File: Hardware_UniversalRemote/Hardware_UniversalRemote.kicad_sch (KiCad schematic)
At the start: 58 parts, among them J1 USB_B_Micro, Q1 S8050, Q2 BSS138, Q3 S8050, Q4 S8050, Q5 S8050, Q6 S8050, Q7 S8050, SW1 SW_Push, SW2 SW_Push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

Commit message: add first pcb layout version
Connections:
- net IO13: now also Q2.2 (S), R8.1, TP2.1; no longer C11.1, R16.2, SW3.1
- net IO16: now also C11.1, R16.2, SW3.1; no longer Q2.2 (S), R8.1, TP2.1
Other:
- moved on the sheet: TP2
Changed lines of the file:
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@@
 	(wire
 		(pts
+			(xy 86.36 137.16) (xy 100.33 137.16)
+		)
+		(stroke
+			(width 0)
+			(type default)
+		)
+	)
+	(wire
+		(pts
 			(xy 234.95 88.9) (xy 234.95 92.71)
 		)
@@
 	(wire
 		(pts
-			(xy 86.36 137.16) (xy 102.87 137.16)
-		)
-		(stroke
-			(width 0)
-			(type default)
-		)
-	)
-	(wire
-		(pts
 			(xy 250.19 140.97) (xy 250.19 142.24)
 		)
@@
 	)
 	(label "KEY"
-		(at 100.33 129.54 180)
+		(at 100.33 137.16 180)
 		(fields_autoplaced yes)
 		(effects
@@
 	)
 	(label "IRM"
-		(at 100.33 137.16 180)
+		(at 100.33 129.54 180)
 		(fields_autoplaced yes)
 		(effects
@@
 	(symbol
 		(lib_id "Connector:TestPoint")
-		(at 102.87 137.16 270)
+		(at 100.33 129.54 270)
 		(unit 1)
 		(exclude_from_sim no)
@@
 		(fields_autoplaced yes)
 		(property "Reference" "TP2"
-			(at 107.95 135.8899 90)
+			(at 105.41 128.2699 90)
 			(effects
 				(font
@@
 		)
 		(property "Value" "TestPoint"
-			(at 107.95 138.4299 90)
+			(at 105.41 130.8099 90)
 			(effects
 				(font
@@
 		)
 		(property "Footprint" "TestPoint:TestPoint_Pad_D2.5mm"
-			(at 102.87 142.24 0)
+			(at 100.33 134.62 0)
 			(effects
 				(font
@@
 		)
 		(property "Datasheet" "~"
-			(at 102.87 142.24 0)
+			(at 100.33 134.62 0)
 			(effects
 				(font
@@
 		)
 		(property "Description" "test point"
-			(at 102.87 137.16 0)
+			(at 100.33 129.54 0)
 			(effects
 				(font

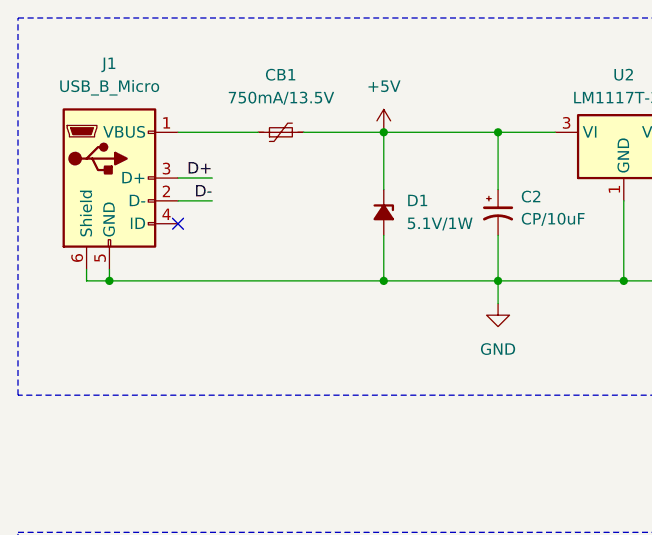
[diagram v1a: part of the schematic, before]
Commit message: modify layout
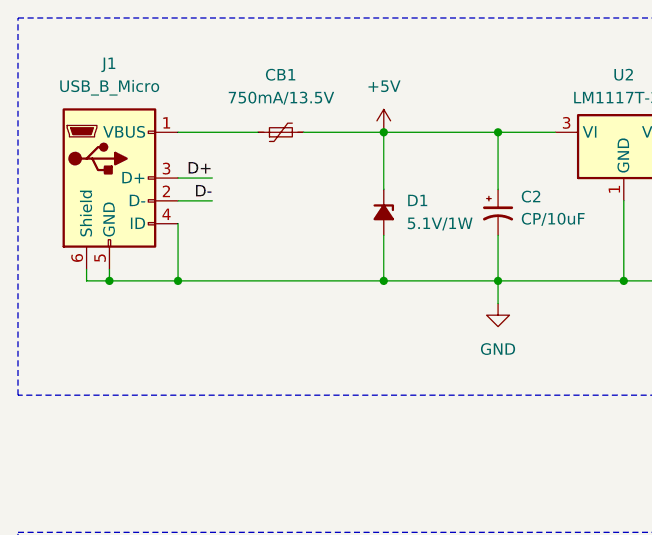
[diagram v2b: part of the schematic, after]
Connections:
- net GND: now also J1.4 (ID)
- no-connect marks 29 -> 28
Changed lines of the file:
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@@
+	)
+	(junction
+		(at 39.37 46.99)
+		(diameter 0)
+		(color 0 0 0 0)
 	)
 	(junction
@@
 	)
 	(no_connect
-		(at 39.37 40.64)
-	)
-	(no_connect
 		(at 95.25 162.56)
 	)
@@
 	(wire
 		(pts
+			(xy 39.37 40.64) (xy 39.37 46.99)
+		)
+		(stroke
+			(width 0)
+			(type default)
+		)
+	)
+	(wire
+		(pts
 			(xy 160.02 165.1) (xy 160.02 154.94)
 		)
@@
 	(wire
 		(pts
+			(xy 39.37 46.99) (xy 31.75 46.99)
+		)
+		(stroke
+			(width 0)
+			(type default)
+		)
+	)
+	(wire
+		(pts
 			(xy 142.24 95.25) (xy 142.24 97.79)
 		)
@@
 	(wire
 		(pts
-			(xy 62.23 46.99) (xy 31.75 46.99)
-		)
-		(stroke
+			(xy 62.23 46.99) (xy 39.37 46.99)
+		)
+		(stroke

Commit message: modify routing
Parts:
- D4, D5, D6, D7, D8, D9: footprint LED_THT:LED_D5.0mm -> LED_THT:LED_D5.0mm_Horizontal_O3.81mm_Z9.0mm
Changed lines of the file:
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@@
 			)
 		)
-		(property "Footprint" "LED_THT:LED_D5.0mm"
+		(property "Footprint" "LED_THT:LED_D5.0mm_Horizontal_O3.81mm_Z9.0mm"
 			(at 189.23 38.1 0)
 			(effects
@@
 			)
 		)
-		(property "Footprint" "LED_THT:LED_D5.0mm"
+		(property "Footprint" "LED_THT:LED_D5.0mm_Horizontal_O3.81mm_Z9.0mm"
 			(at 189.23 46.99 0)
 			(effects
@@
 			)
 		)
-		(property "Footprint" "LED_THT:LED_D5.0mm"
+		(property "Footprint" "LED_THT:LED_D5.0mm_Horizontal_O3.81mm_Z9.0mm"
 			(at 255.27 38.1 0)
 			(effects
@@
 			)
 		)
-		(property "Footprint" "LED_THT:LED_D5.0mm"
+		(property "Footprint" "LED_THT:LED_D5.0mm_Horizontal_O3.81mm_Z9.0mm"
 			(at 223.52 38.1 0)
 			(effects
@@
 			)
 		)
-		(property "Footprint" "LED_THT:LED_D5.0mm"
+		(property "Footprint" "LED_THT:LED_D5.0mm_Horizontal_O3.81mm_Z9.0mm"
 			(at 255.27 46.99 0)
 			(effects
@@
 			)
 		)
-		(property "Footprint" "LED_THT:LED_D5.0mm"
+		(property "Footprint" "LED_THT:LED_D5.0mm_Horizontal_O3.81mm_Z9.0mm"
 			(at 223.52 46.99 0)
 			(effects

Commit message: add trace
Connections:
- net +3.3V: now also C3.1, C4.1, U1.2 (VDD)
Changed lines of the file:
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@@
 	)
 	(junction
+		(at 71.12 85.09)
+		(diameter 0)
+		(color 0 0 0 0)
+	)
+	(junction
 		(at 71.12 96.52)
 		(diameter 0)
@@
 	(wire
 		(pts
+			(xy 71.12 82.55) (xy 71.12 85.09)
+		)
+		(stroke
+			(width 0)
+			(type default)
+		)
+	)
+	(wire
+		(pts
 			(xy 34.29 97.79) (xy 34.29 100.33)
 		)
@@
 					(unit 1)
 				)
+			)
+		)
+	)
+	(symbol
+		(lib_id "power:+3.3V")
+		(at 71.12 82.55 0)
+		(unit 1)
+		(exclude_from_sim no)
+		(in_bom yes)
+		(on_board yes)
+		(dnp no)
+		(fields_autoplaced yes)
+		(property "Reference" "#PWR024"
+			(at 71.12 86.36 0)
+			(effects
+				(font
+					(size 1.27 1.27)
+				)
+				(hide yes)
+			)
+		)
+		(property "Value" "+3.3V"
+			(at 71.12 77.47 0)
+			(effects
+				(font
+					(size 1.27 1.27)
+				)
+			)
+		)
+		(property "Footprint" ""
+			(at 71.12 82.55 0)
+			(effects
+				(font
+					(size 1.27 1.27)
+				)
+				(hide yes)
+			)
+		)
+		(property "Datasheet" ""
+			(at 71.12 82.55 0)
+			(effects
+				(font
+					(size 1.27 1.27)
+				)
+				(hide yes)
+			)
+		)
+		(property "Description" "Power symbol creates a global label with name \"+3.3V\""
+			(at 71.12 82.55 0)
+			(effects
+				(font
+					(size 1.27 1.27)
+				)
+				(hide yes)
+			)
+		)
+		(pin "1"
+		)
+		(instances
+			(project "Hardware_UniversalRemote"
+				(path "/afb609ba-90f2-4616-a61f-4359f566cfcc"
+					(reference "#PWR024")
+					(unit 1)
+				)

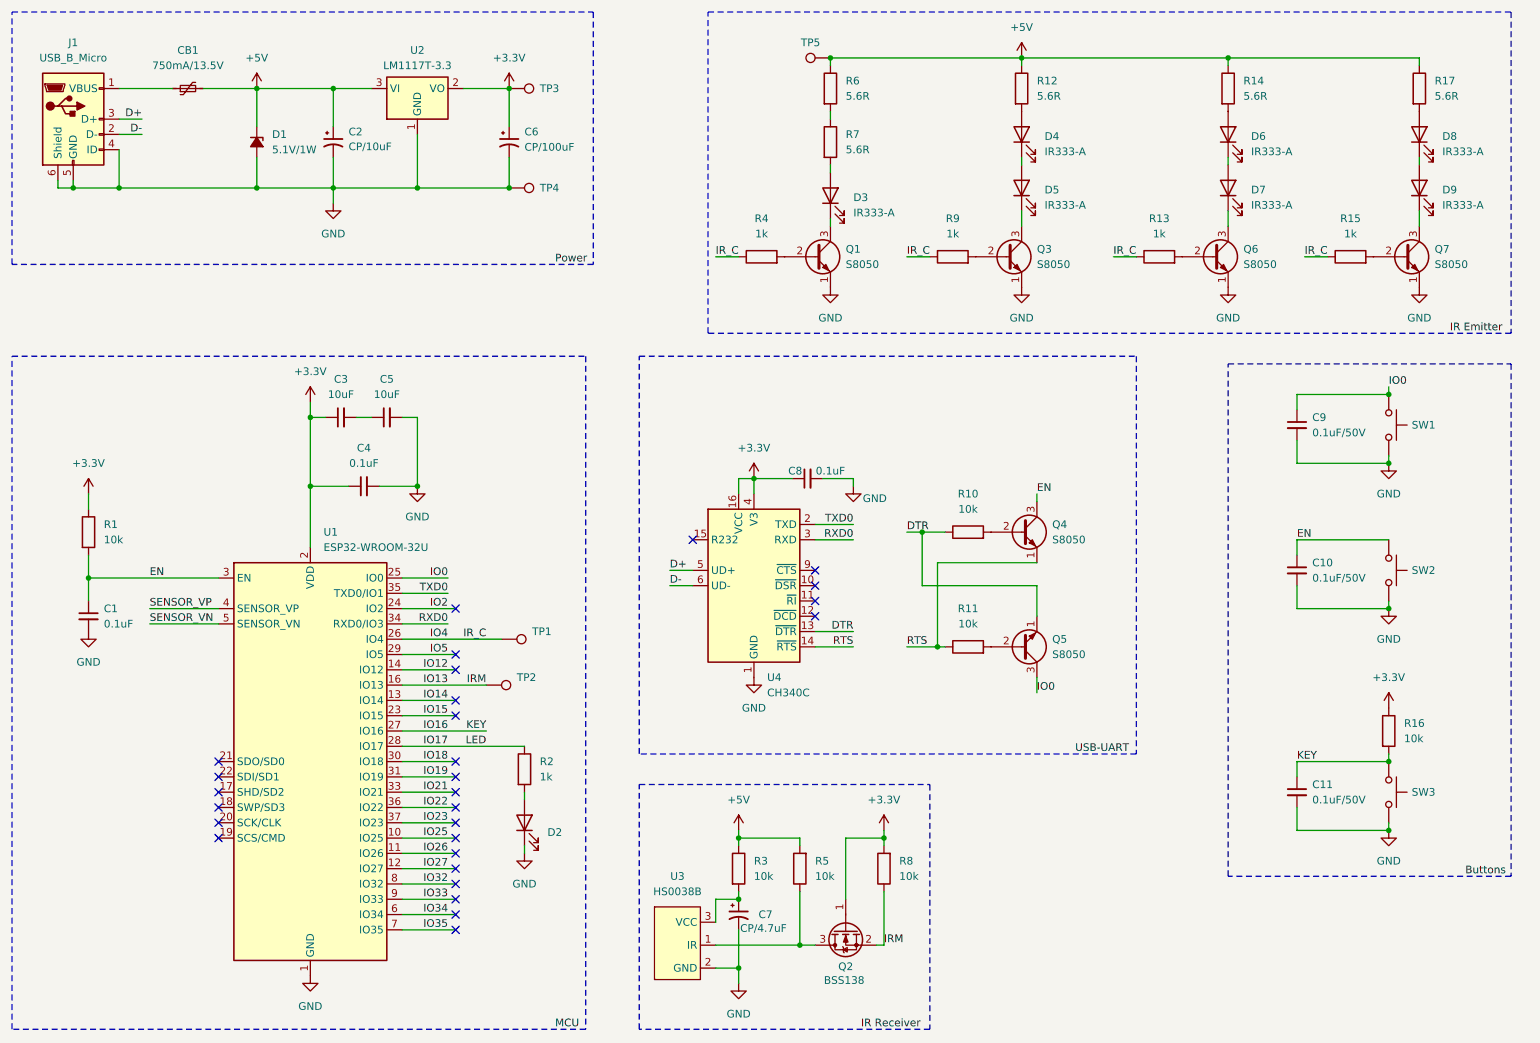
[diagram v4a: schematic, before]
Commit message: fix txd/rxd routing for mcu flashing
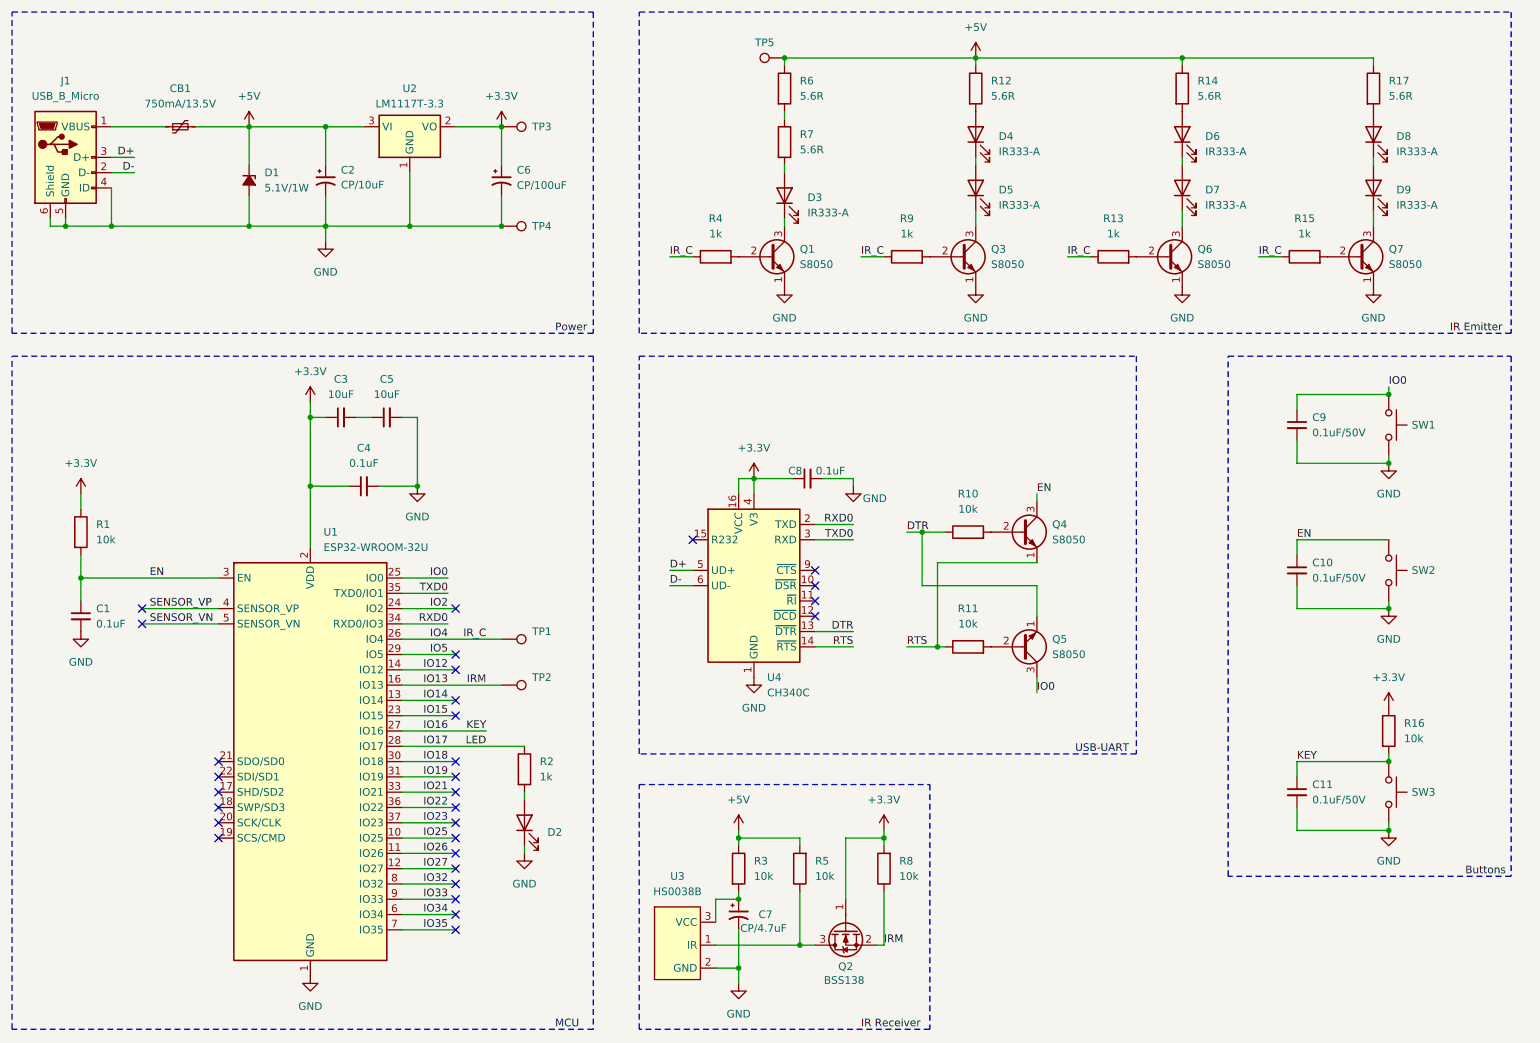
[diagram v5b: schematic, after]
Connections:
- net RXD0: now also U4.2 (TXD); no longer U4.3 (RXD)
- net TXD0: now also U4.3 (RXD); no longer U4.2 (TXD)
- no-connect marks 28 -> 30
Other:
- moved on the sheet: C1, C2, C6, CB1, D1, D3, D4, D5, D6, D7, D8, D9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
